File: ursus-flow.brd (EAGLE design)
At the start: 92.7 x 50.8 mm, 65 parts

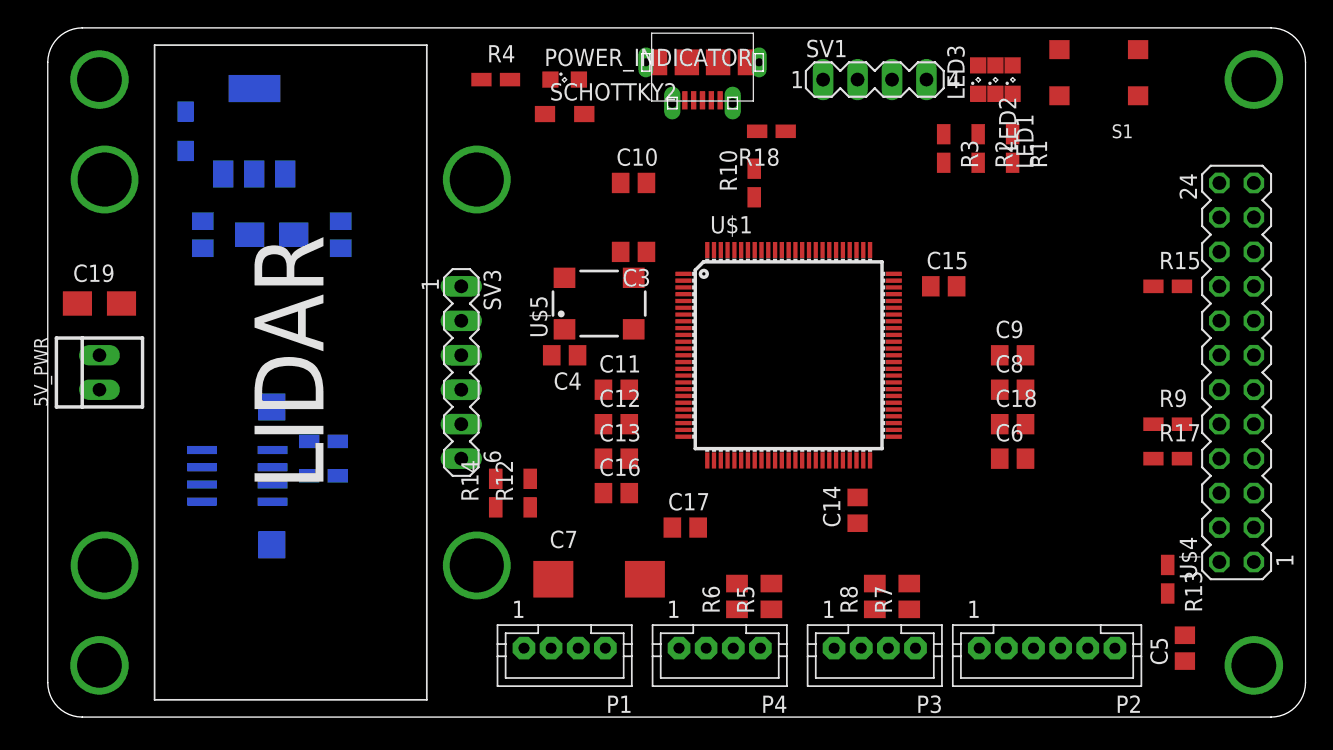
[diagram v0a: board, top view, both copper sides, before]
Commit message: Add MPU9250 breakout board
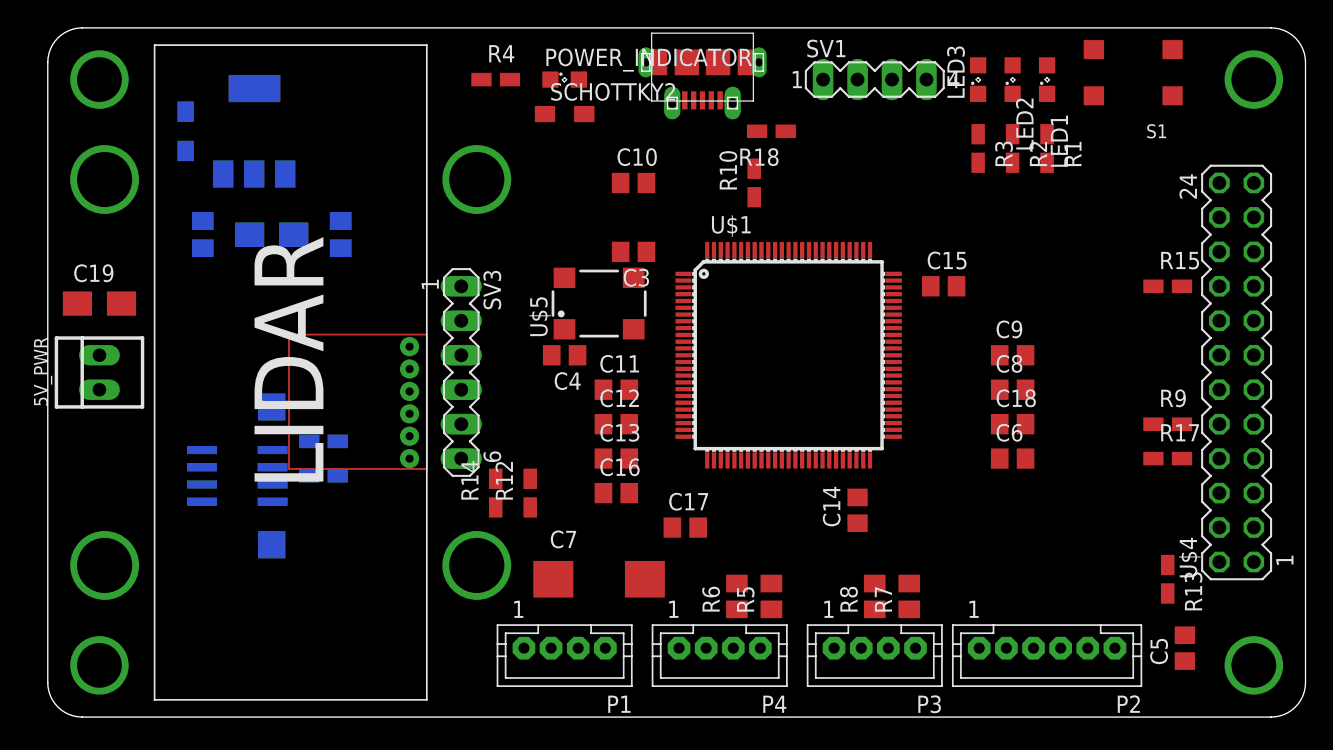
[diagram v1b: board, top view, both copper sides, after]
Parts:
- added U$11: MPU9250_BREAKOUT, MPU9250_BREAKOUT:MPU9250_BREAKOUT
- moved LED1 2.54 mm to (74.9, 76.2)
- moved R1 2.54 mm to (74.9, 71.1)
- moved R2 2.54 mm to (72.4, 71.1)
- moved S1 2.54 mm to (81.3, 76.7)
- moved R3 2.54 mm to (69.8, 71.1)
- moved LED2 1.27 mm to (72.4, 76.2)
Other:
- board text added: "Computer vision board"
- board text added: "Ursus-flow"
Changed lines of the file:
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@@
 <layer number="103" name="tMap" color="7" fill="1" visible="no" active="yes"/>
 <layer number="104" name="Name" color="16" fill="1" visible="no" active="yes"/>
-<layer number="105" name="tPlate" color="7" fill="1" visible="no" active="yes"/>
-<layer number="106" name="bPlate" color="7" fill="1" visible="no" active="yes"/>
+<layer number="105" name="tPlate" color="7" fill="1" visible="yes" active="yes"/>
+<layer number="106" name="bPlate" color="7" fill="1" visible="yes" active="yes"/>
 <layer number="107" name="Crop" color="7" fill="1" visible="no" active="yes"/>
 <layer number="116" name="Patch_BOT" color="9" fill="4" visible="no" active="yes"/>
@@
 <board>
 <plain>
-<wire x1="3.81" y1="29.21" x2="91.44" y2="29.21" width="0" layer="20"/>
-<wire x1="93.98" y1="31.75" x2="93.98" y2="77.47" width="0" layer="20"/>
 <wire x1="1.27" y1="77.47" x2="1.27" y2="31.75" width="0" layer="20"/>
 <wire x1="1.27" y1="77.47" x2="3.81" y2="80.01" width="0" layer="20" curve="-90"/>
 <wire x1="3.81" y1="29.21" x2="1.27" y2="31.75" width="0" layer="20" curve="-90"/>
-<wire x1="3.81" y1="80.01" x2="91.44" y2="80.01" width="0" layer="20"/>
 <dimension x1="1.27" y1="80.01" x2="1.27" y2="29.21" x3="-2.54" y3="54.61" textsize="1.778" layer="1"/>
 <dimension x1="1.27" y1="80.01" x2="93.98" y2="80.01" x3="47.625" y3="83.82" textsize="1.778" layer="1"/>
 <wire x1="91.44" y1="80.01" x2="93.98" y2="77.47" width="0" layer="20" curve="-90"/>
 <wire x1="93.98" y1="31.75" x2="91.44" y2="29.21" width="0" layer="20" curve="-90"/>
+<wire x1="3.81" y1="80.01" x2="91.44" y2="80.01" width="0" layer="20"/>
+<wire x1="93.98" y1="77.47" x2="93.98" y2="31.75" width="0" layer="20"/>
+<wire x1="3.81" y1="29.21" x2="91.44" y2="29.21" width="0" layer="20"/>
+<text x="64.77" y="58.42" size="5.08" layer="106" rot="MR0">Ursus-flow</text>
+<text x="59.69" y="54.61" size="1.778" layer="106" rot="MR0">Computer vision board</text>
 </plain>
 <attributes>
@@
 <element name="C8" library="rcl" package="C0805" value="0.1uf" x="72.39" y="53.34"/>
 <element name="C9" library="rcl" package="C0805" value="0.1uf" x="72.39" y="55.88"/>
-<element name="LED1" library="led" package="SML0805" value="" x="72.39" y="76.2" smashed="yes" rot="R90">
-<attribute name="NAME" x="73.93" y="69.62" size="1.27" layer="25" rot="R90"/>
+<element name="LED1" library="led" package="SML0805" value="" x="74.93" y="76.2" smashed="yes" rot="R90">
+<attribute name="NAME" x="76.47" y="69.62" size="1.27" layer="25" rot="R90"/>
+<attribute name="VALUE" x="76.93" y="74.7" size="1.27" layer="27" rot="R90"/>
+</element>
+<element name="LED2" library="led" package="SML0805" value="" x="72.39" y="76.2" smashed="yes" rot="R90">
+<attribute name="NAME" x="73.93" y="70.89" size="1.27" layer="25" rot="R90"/>
 <attribute name="VALUE" x="74.39" y="74.7" size="1.27" layer="27" rot="R90"/>
-</element>
-<element name="LED2" library="led" package="SML0805" value="" x="71.12" y="76.2" smashed="yes" rot="R90">
-<attribute name="NAME" x="72.66" y="70.89" size="1.27" layer="25" rot="R90"/>
-<attribute name="VALUE" x="73.12" y="74.7" size="1.27" layer="27" rot="R90"/>
 </element>
 <element name="LED3" library="led" package="SML0805" value="" x="69.85" y="76.2" rot="R90"/>
@@
 <element name="P4" library="jst-ph" package="JST-PH4" value="" x="50.8" y="34.29" rot="R180"/>
 <element name="POWER_INDICATOR" library="led" package="SML0805" value="" x="39.37" y="76.2"/>
-<element name="R1" library="resistor" package="R0805W" value="220" x="72.39" y="71.12" rot="R270"/>
+<element name="R1" library="resistor" package="R0805W" value="220" x="74.93" y="71.12" rot="R270"/>
 <element name="R10" library="resistor" package="R0805W" value="10k" x="53.34" y="68.58" rot="R90"/>
 <element name="R11" library="resistor" package="R0805W" value="4.7k" x="21.59" y="46.99" rot="MR0"/>
@@
 <element name="R17" library="resistor" package="R0805W" value="10k" x="83.82" y="48.26"/>
 <element name="R18" library="resistor" package="R0805W" value="1k" x="54.61" y="72.39" rot="R180"/>
-<element name="R2" library="resistor" package="R0805W" value="220" x="69.85" y="71.12" rot="R270"/>
-<element name="R3" library="resistor" package="R0805W" value="220" x="67.31" y="71.12" rot="R270"/>
+<element name="R2" library="resistor" package="R0805W" value="220" x="72.39" y="71.12" rot="R270"/>
+<element name="R3" library="resistor" package="R0805W" value="220" x="69.85" y="71.12" rot="R270"/>
 <element name="R4" library="resistor" package="R0805W" value="220" x="34.29" y="76.2"/>
 <element name="R5" library="rcl" package="M0805" value="1k" x="54.61" y="38.1" rot="R90"/>
@@
 <element name="R8" library="rcl" package="M0805" value="1k" x="62.23" y="38.1" rot="R90"/>
 <element name="R9" library="resistor" package="R0805W" value="10k" x="83.82" y="50.8"/>
-<element name="S1" library="switch-panasonic" package="EVQPSL/Q" value="EVQPSL/Q" x="78.74" y="76.708" rot="R90"/>
+<element name="S1" library="switch-panasonic" package="EVQPSL/Q" value="EVQPSL/Q" x="81.28" y="76.708" rot="R90"/>
 <element name="SCHOTTKY1" library="_mod_diode" package="SOD323-W" value="NSVR0320MW2T1G" x="11.43" y="72.39" rot="MR90"/>
 <element name="SCHOTTKY2" library="_mod_diode" package="SOD323-W" value="NSVR0320MW2T1G" x="39.37" y="73.66"/>
@@
 <element name="U$9" library="M3_HOLE" package="M3_HOLE" value="M3_HOLE" x="5.08" y="76.2"/>
 <element name="U$10" library="M3_HOLE" package="M3_HOLE" value="M3_HOLE" x="90.17" y="76.2"/>
+<element name="U$11" library="MPU9250_BREAKOUT" package="MPU9250_BREAKOUT" value="MPU9250_BREAKOUT" x="27.94" y="48.26" rot="R90"/>
 </elements>
 <signals>
@@
 <contactref element="R1" pad="2"/>
 <contactref element="LED1" pad="C"/>
-<wire x1="72.39" y1="70.0675" x2="72.39" y2="75.15" width="0" layer="19" extent="1-1"/>
+<wire x1="74.93" y1="70.0675" x2="74.93" y2="75.15" width="0" layer="19" extent="1-1"/>
 </signal>
 <signal name="N$2">
 <contactref element="LED2" pad="C"/>
 <contactref element="R2" pad="2"/>
-<wire x1="69.85" y1="70.0675" x2="71.12" y2="75.15" width="0" layer="19" extent="1-1"/>
+<wire x1="72.39" y1="70.0675" x2="72.39" y2="75.15" width="0" layer="19" extent="1-1"/>
 </signal>
 <signal name="N$3">
 <contactref element="LED3" pad="C"/>
 <contactref element="R3" pad="2"/>
-<wire x1="69.85" y1="75.15" x2="67.31" y2="70.0675" width="0" layer="19" extent="1-1"/>
+<wire x1="69.85" y1="75.15" x2="69.85" y2="70.0675" width="0" layer="19" extent="1-1"/>
 </signal>
 <signal name="N$4">
@@
 <wire x1="79.93" y1="34.29" x2="53.705" y2="77.47" width="0" layer="19" extent="1-1"/>
 <wire x1="36.37" y1="34.29" x2="79.93" y2="34.29" width="0" layer="19" extent="1-1"/>
-<wire x1="81.64" y1="78.408" x2="79.93" y2="34.29" width="0" layer="19" extent="1-1"/>
-<wire x1="75.84" y1="78.408" x2="81.64" y2="78.408" width="0" layer="19" extent="1-1"/>
-<wire x1="38.535" y1="39.37" x2="81.64" y2="78.408" width="0" layer="19" extent="1-1"/>
+<wire x1="84.18" y1="78.408" x2="79.93" y2="34.29" width="0" layer="19" extent="1-1"/>
+<wire x1="78.38" y1="78.408" x2="84.18" y2="78.408" width="0" layer="19" extent="1-1"/>
+<wire x1="38.535" y1="39.37" x2="84.18" y2="78.408" width="0" layer="19" extent="1-1"/>
 <wire x1="16.155" y1="64.77" x2="38.535" y2="39.37" width="0" layer="19" extent="1-1"/>
 <wire x1="17.84" y1="46.355" x2="16.155" y2="64.77" width="0" layer="19" extent="1-1"/>
@@
 <wire x1="61.38" y1="48.13" x2="49.88" y2="48.13" width="0" layer="19" extent="1-1"/>
 <wire x1="63.63" y1="61.38" x2="50.38" y2="63.63" width="0" layer="19" extent="1-1"/>
-<wire x1="72.39" y1="72.1725" x2="16.155" y2="64.77" width="0" layer="19" extent="1-1"/>
+<wire x1="74.93" y1="72.1725" x2="16.155" y2="64.77" width="0" layer="19" extent="1-1"/>
+<wire x1="72.39" y1="72.1725" x2="74.93" y2="72.1725" width="0" layer="19" extent="1-1"/>
+<wire x1="44.46" y1="57.79" x2="72.39" y2="72.1725" width="0" layer="19" extent="1-1"/>
 <wire x1="69.85" y1="72.1725" x2="72.39" y2="72.1725" width="0" layer="19" extent="1-1"/>
-<wire x1="44.46" y1="57.79" x2="69.85" y2="72.1725" width="0" layer="19" extent="1-1"/>
-<wire x1="67.31" y1="72.1725" x2="69.85" y2="72.1725" width="0" layer="19" extent="1-1"/>
-<wire x1="33.2375" y1="76.2" x2="67.31" y2="72.1725" width="0" layer="19" extent="1-1"/>
+<wire x1="33.2375" y1="76.2" x2="69.85" y2="72.1725" width="0" layer="19" extent="1-1"/>
 <wire x1="39.36" y1="61.59" x2="44.46" y2="57.79" width="0" layer="19" extent="1-1"/>
 <wire x1="12.7" y1="63.77" x2="39.36" y2="61.59" width="0" layer="19" extent="1-1"/>
@@
 <contactref element="U$1" pad="60"/>
 <contactref element="LED2" pad="A"/>
-<wire x1="71.12" y1="77.25" x2="63.63" y2="54.38" width="0" layer="19" extent="1-1"/>
+<wire x1="72.39" y1="77.25" x2="63.63" y2="54.38" width="0" layer="19" extent="1-1"/>
 </signal>
 <signal name="LED_R">
 <contactref element="U$1" pad="61"/>
 <contactref element="LED1" pad="A"/>
-<wire x1="63.63" y1="54.88" x2="72.39" y2="77.25" width="0" layer="19" extent="1-1"/>
+<wire x1="63.63" y1="54.88" x2="74.93" y2="77.25" width="0" layer="19" extent="1-1"/>
 </signal>
 <signal name="AT24C08C_A2">
@@
 <contactref element="S1" pad="A1"/>
 <contactref element="S1" pad="A"/>
-<wire x1="75.84" y1="75.008" x2="81.64" y2="75.008" width="0" layer="19" extent="1-1"/>
-<wire x1="47.31" y1="43.18" x2="75.84" y2="75.008" width="0" layer="19" extent="1-1"/>
+<wire x1="78.38" y1="75.008" x2="84.18" y2="75.008" width="0" layer="19" extent="1-1"/>
+<wire x1="47.31" y1="43.18" x2="78.38" y2="75.008" width="0" layer="19" extent="1-1"/>
 </signal>
 <signal name="N$17">

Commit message: Update MT9V034 and MPU9250
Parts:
- removed C18, C5: 0.1uf, rcl:C0805
- removed R17, R9: 10k, resistor:R0805W
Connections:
- removed net N$17: R9.1, U$4.10
- removed net N$18: R17.1, U$4.8
- net +3V3: no longer C18.1, R17.2, R9.2
- net +5V: no longer C5.2
- net GND: no longer C18.2, C5.1, U$4.7, U$4.9

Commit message: Arrange components
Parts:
- PWR_LED: value (none) -> PWR_LED
- S1: value EVQPSL/Q -> (none)
- SCHOTTKY1: value NSVR0320MW2T1G -> shottky1
- SCHOTTKY2: value NSVR0320MW2T1G -> shottky2
- moved U$11 17.3 mm to (22.9, 31.8)
- moved C6 5.08 mm to (72.4, 53.3)
- moved C8 2.54 mm to (72.4, 55.9)
- moved C9 2.54 mm to (72.4, 58.4)
- moved R13 1.80 mm to (82.5, 40.6)
- renumbered P1 to [LIDAR], P2 to [SPI2], P3 to [UART2], P4 to [UART3], POWER_INDICATOR to PWR_LED, SV1 to [ST-LINK]
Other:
- board size 92.7 x 50.8 mm -> 92.8 x 50.9 mm

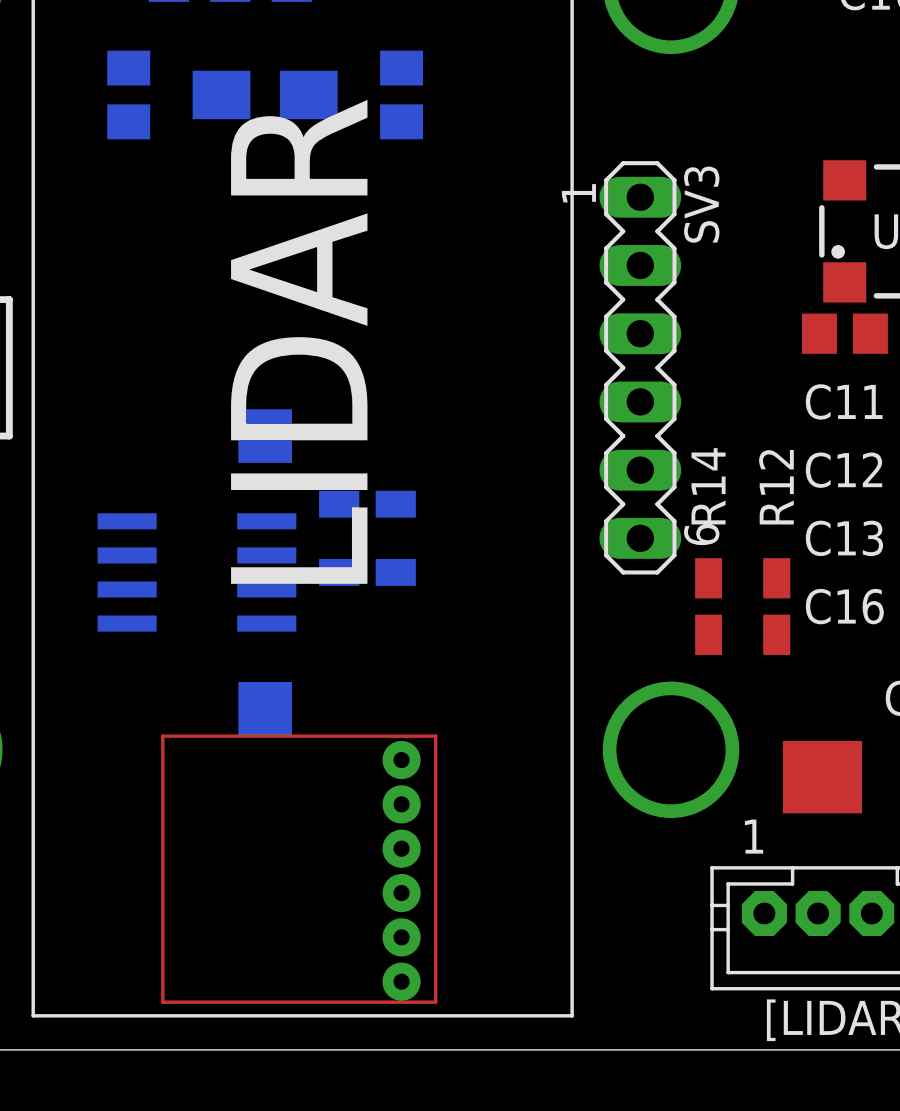
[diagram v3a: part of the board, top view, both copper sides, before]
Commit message: Remove wrong footprint of MPU9250
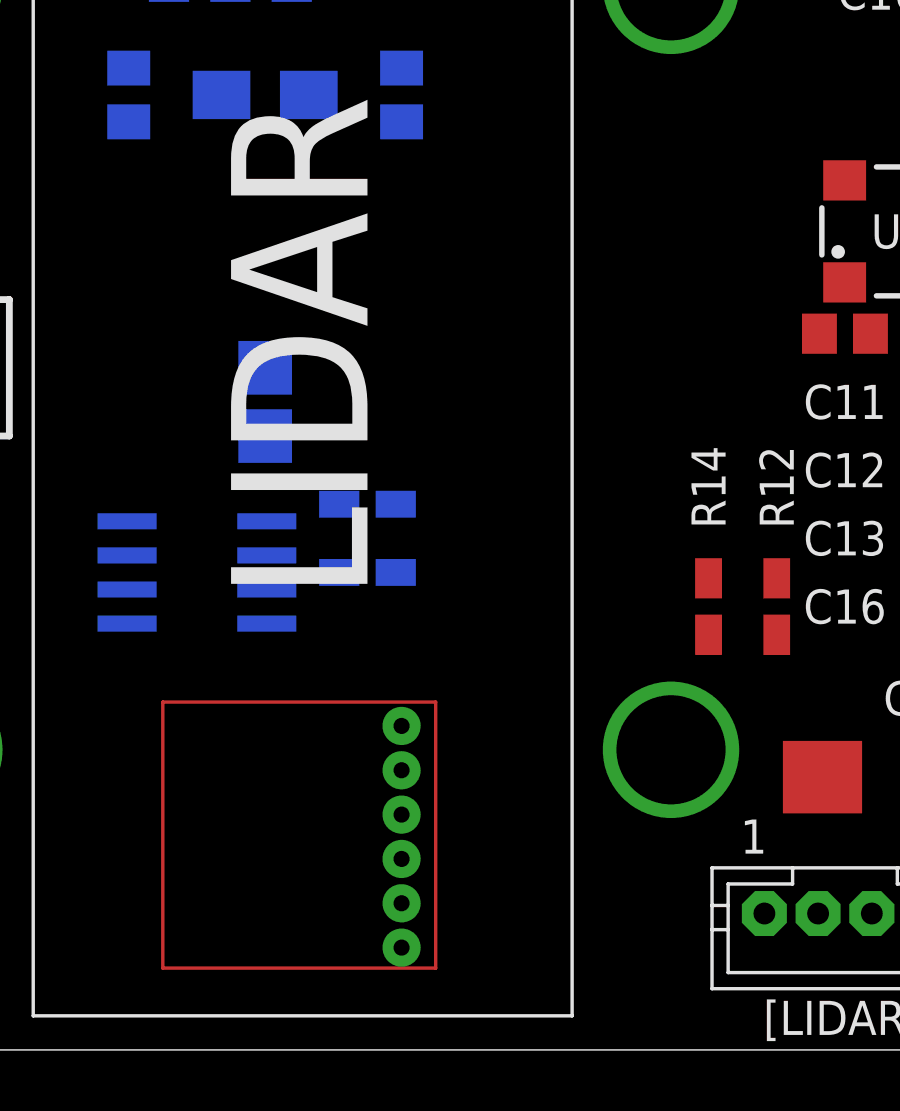
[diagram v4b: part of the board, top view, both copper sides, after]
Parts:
- removed SV3: (no value), con-lstb:MA06-1
- removed TEST_PAD2: TPSQTP20SQ, testpad:TP20SQ
- added I2C3_SDA: TPSQTP20SQ, testpad:TP20SQ
- moved U$11 1.27 mm to (22.9, 33.0)
- renumbered TEST_PAD1 to I2C3_SCL
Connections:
- net +3V3: now also U$11.P$1; no longer SV3.6
- net AT24C08C_I2C3_SCL: now also I2C3_SCL.TP; no longer TEST_PAD2.TP
- net AT24C08C_I2C3_SDA: now also I2C3_SDA.TP; no longer I2C3_SCL.TP
- net GND: now also U$11.P$2; no longer SV3.5
- net MPU9250_SPI1_CS: now also U$11.P$3; no longer SV3.4
- net MPU9250_SPI1_MISO: now also U$11.P$6; no longer SV3.1
- net MPU9250_SPI1_MOSI: now also U$11.P$5; no longer SV3.2
- net MPU9250_SPI1_SCK: now also U$11.P$4; no longer SV3.3

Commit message: Start doing PCB layout
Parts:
- LED1: value (none) -> R
- LED2: value (none) -> G
- LED3: value (none) -> B
- [LIDAR]: value (none) -> lidar_connector
- [SPI2]: value (none) -> spi2_connector
- [ST-LINK]: value (none) -> stlink_connector
- [UART2]: value (none) -> uart2_connector
- [UART3]: value (none) -> uart3_connector
- moved C6 51.5 mm to (21.6, 44.7), flipped to the bottom, turned to 180 degrees
- moved C8 25.7 mm to (48.8, 45.7)
- moved C13 20.7 mm to (63.8, 46.2), turned to 180 degrees
- moved R13 20.1 mm to (89.7, 59.4), flipped to the bottom, turned to 90 degrees
- moved C17 12.0 mm to (44.5, 54.6), turned to 180 degrees
- moved C11 9.57 mm to (52.1, 56.9), flipped to the bottom
- moved C9 9.16 mm to (64.8, 63.5), turned to 180 degrees
- moved U$11 8.89 mm to (22.9, 41.9), flipped to the bottom, turned to 270 degrees
- moved R14 8.41 mm to (38.4, 38.4), turned to 270 degrees
- moved R12 8.18 mm to (40.4, 38.4), turned to 270 degrees
- moved C15 6.48 mm to (73.7, 62.2)
- moved C16 4.83 mm to (43.2, 50.5), turned to 180 degrees
- moved C10 4.58 mm to (48.3, 66.0), turned to 270 degrees
- moved R15 4.37 mm to (80.3, 58.4), flipped to the bottom, turned to 180 degrees
- moved U$4 3.81 mm to (85.1, 54.6)
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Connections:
- removed net N$16: C17.1, S1.A, S1.A1
- removed net N$5: C10.1, C11.1, C12.1, C13.1, C8.1, C9.1
- net AT24C08C_A2: now also U$1.62
- net DCMI_D3: now also U$1.98; no longer U$1.97
- net DCMI_PIXCLK: now also U$4.21
- net GND: now also C10.1, C11.1, C12.1, C13.1, C8.1, C9.1
- net NRST: now also C17.1, S1.A, S1.A1
- net UART2_RX: now also R8.2
- net UART2_TX: now also R7.2
- net UART3_RX: now also R6.2
- net V_USB: now also R18.1
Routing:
- net GND: track 0.00 -> 241.3 mm, vias 0 -> 1
- net +5V: track 0.00 -> 85.8 mm, vias 0 -> 2
- net DCMI_PIXCLK: track 0.00 -> 78.1 mm, vias 0 -> 1
- net DCMI_D5: track 0.00 -> 65.8 mm
- net DCMI_D3: track 0.00 -> 58.3 mm, vias 0 -> 1
- net DCMI_VSYNC: track 0.00 -> 52.9 mm, vias 0 -> 2
- net DCMI_D9: track 0.00 -> 51.2 mm
- net DCMI_D8: track 0.00 -> 49.5 mm, vias 0 -> 1
- net DCMI_D4: track 0.00 -> 49.2 mm, vias 0 -> 1
- net DCMI_HSYNC: track 0.00 -> 45.8 mm, vias 0 -> 1
- net +3V3: track 0.00 -> 34.7 mm
- net DCMI_D1: track 0.00 -> 32.3 mm
- net DCMI_D0: track 0.00 -> 30.0 mm
- net DCMI_D2: track 0.00 -> 29.4 mm
- net DCMI_SYSCLK: track 0.00 -> 26.3 mm, vias 0 -> 2
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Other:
- board size 92.8 x 50.9 mm -> 90.2 x 50.8 mm
